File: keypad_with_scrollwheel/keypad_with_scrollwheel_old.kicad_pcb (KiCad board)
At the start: 2 copper layers, 40 x 60 mm, 34 parts, among them Q1 BC847, U1 KEYPAD_OVERLAY, U2 SCROLLWHEEL

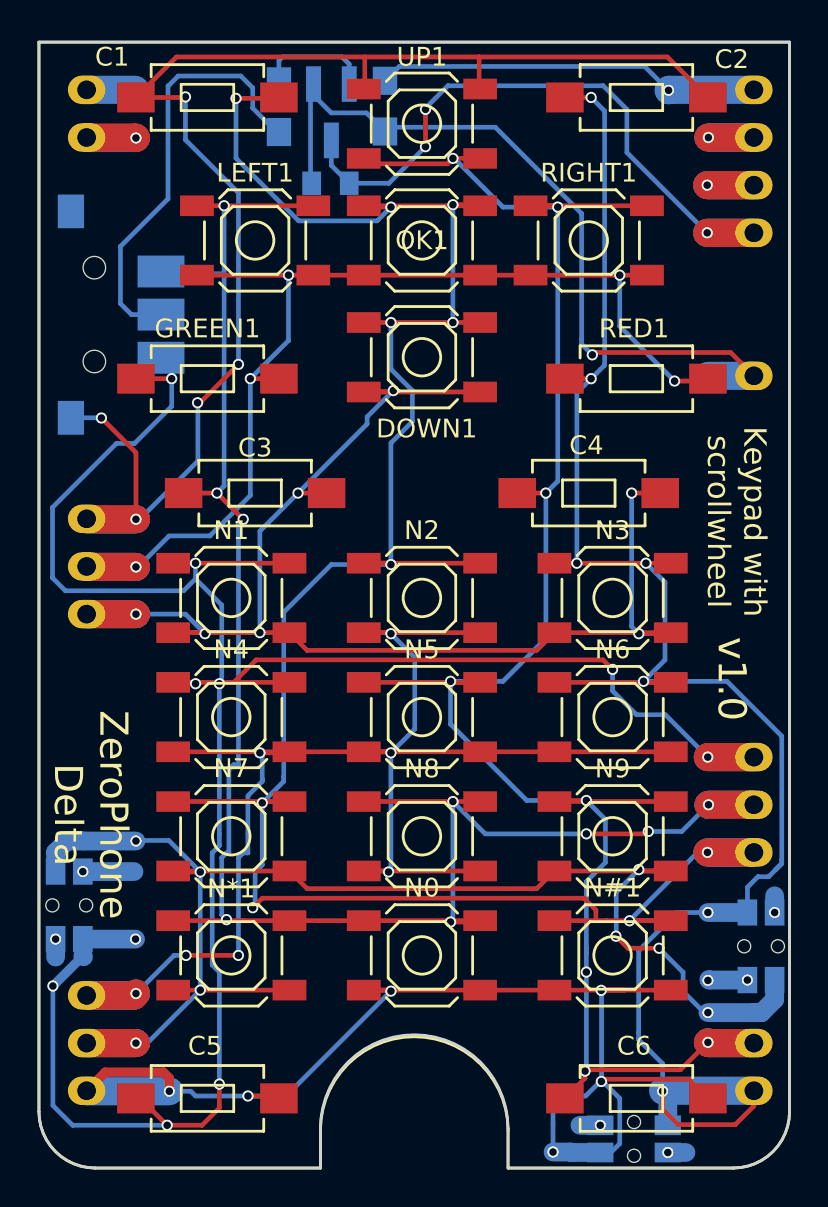
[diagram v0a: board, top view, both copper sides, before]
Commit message: Updating the keypad+scrollwheel board to have correct footprint&stronger traces
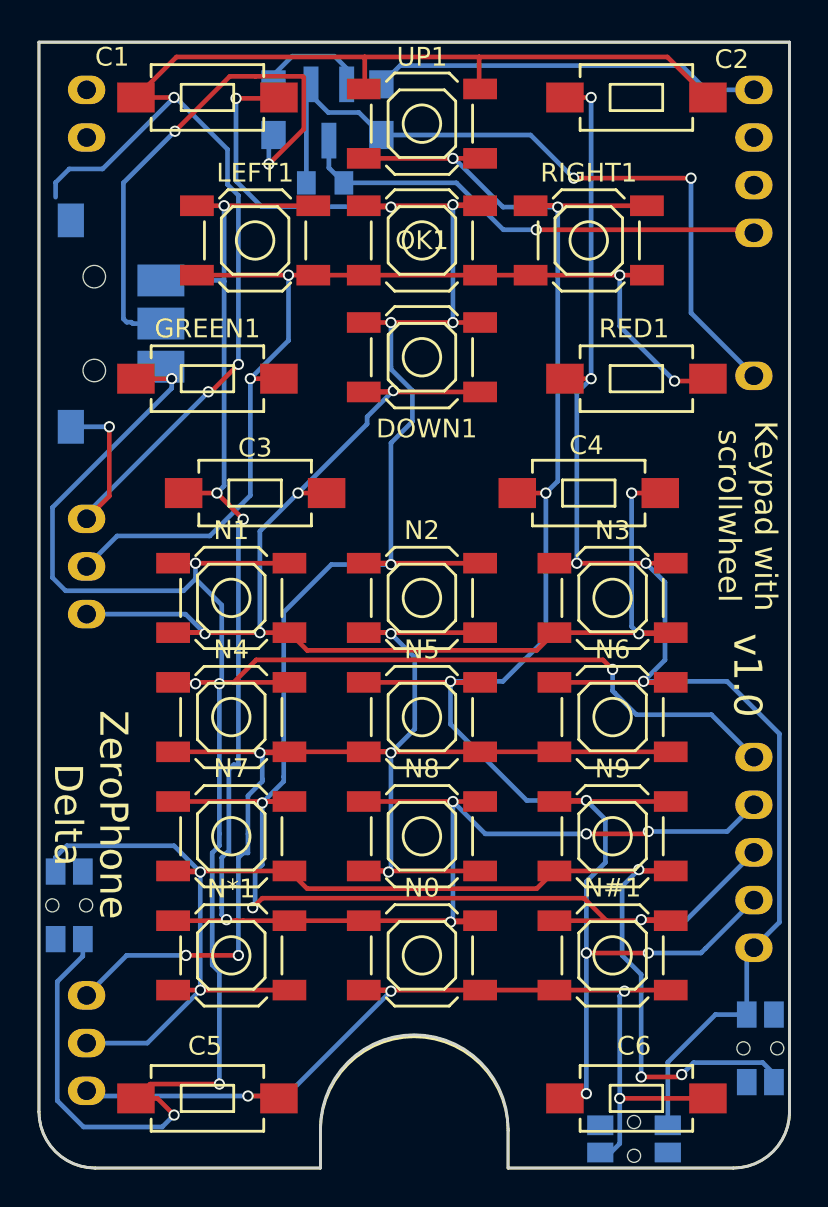
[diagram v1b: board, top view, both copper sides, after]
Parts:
- moved PHOTO1 5.44 mm to (186.9, 158.6)
- moved U2 0.48 mm to (150.2, 120.0)
- moved R1 0.33 mm to (161.0, 108.6)
- moved C7 0.29 mm to (163.8, 112.5)
- moved R2 0.27 mm to (166.8, 108.6)
- moved Q1 0.13 mm to (163.9, 108.8)
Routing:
- net (no net): track 26.4 -> 0.00 mm, vias 10 -> 0
- net /COL6: track 70.2 -> 52.5 mm, vias 6 -> 4
- net /ROW1: track 98.6 -> 81.7 mm, vias 7 -> 5
- net GND: track 35.3 -> 25.5 mm, vias 3 -> 1
- net /COL5: track 87.0 -> 79.5 mm, vias 8 -> 5
- net RIGHT: track 127.0 -> 120.3 mm, vias 10 -> 7
- net PUSH: track 23.0 -> 28.4 mm, vias 0 -> 2
- net COM: track 77.4 -> 81.5 mm, vias 5 -> 4
- net /ROW3: track 127.8 -> 124.4 mm, vias 10 -> 9
- net /COL2: track 60.0 -> 57.1 mm, vias 5 -> 4
- net /COL4: track 81.9 -> 79.1 mm, vias 7 -> 6
- net /COL3: track 74.7 -> 72.1 mm, vias 7 -> 6
- net GPIO: track 42.4 -> 39.9 mm, vias 1 -> 2
- net LEFT: track 101.7 -> 99.8 mm, vias 9 -> 8
- net /ROW2: track 107.9 -> 106.1 mm
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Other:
- board text added: "For assembly, follow directions for the normal keypad boards (available in assembly instructions) Values for SMD resistors/ capacitors are yet to be determined"
- board text removed: "For assembly, follow directions for normal keypad boards (available in assembly instructions)"
- board text removed: "Values for SMD resistors/ capacitors are yet to be determined"
